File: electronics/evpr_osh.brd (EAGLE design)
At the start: 88.4 x 47.3 mm, 137 parts

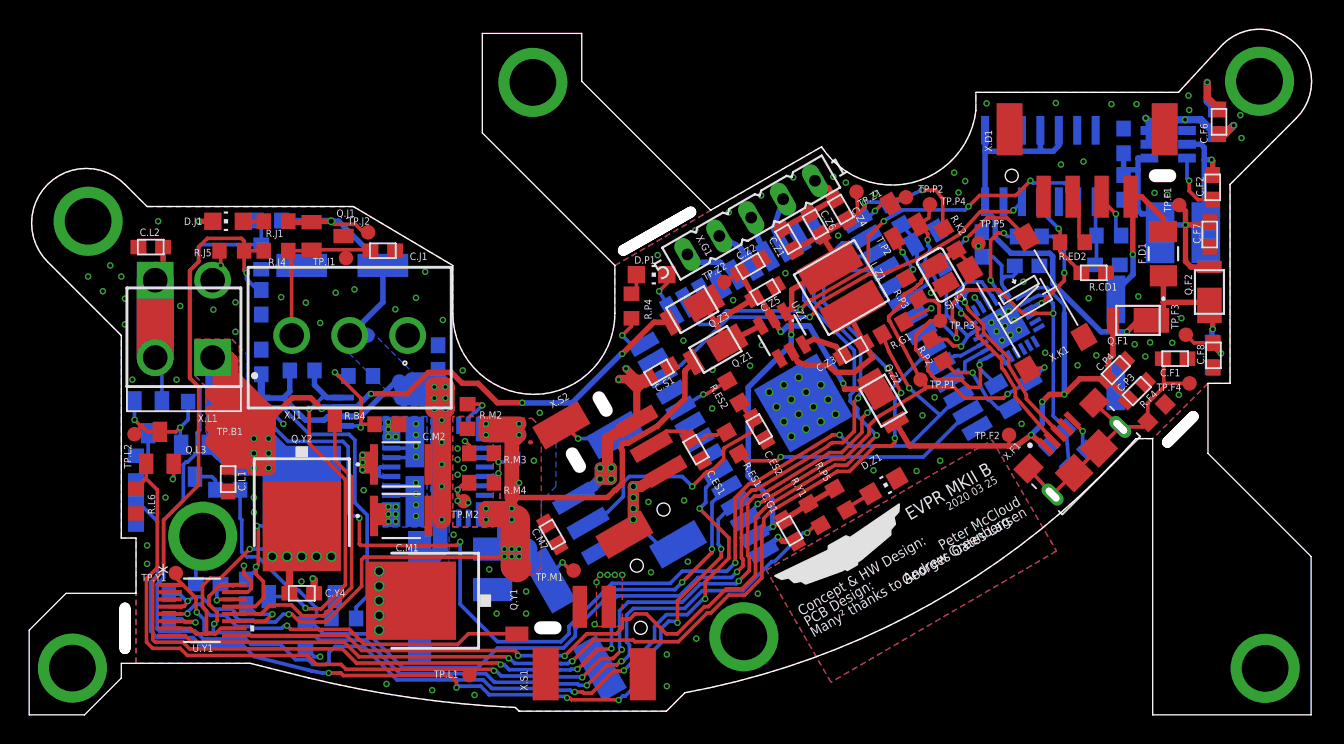
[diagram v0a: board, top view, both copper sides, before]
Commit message: Slightly squeezed board profile down
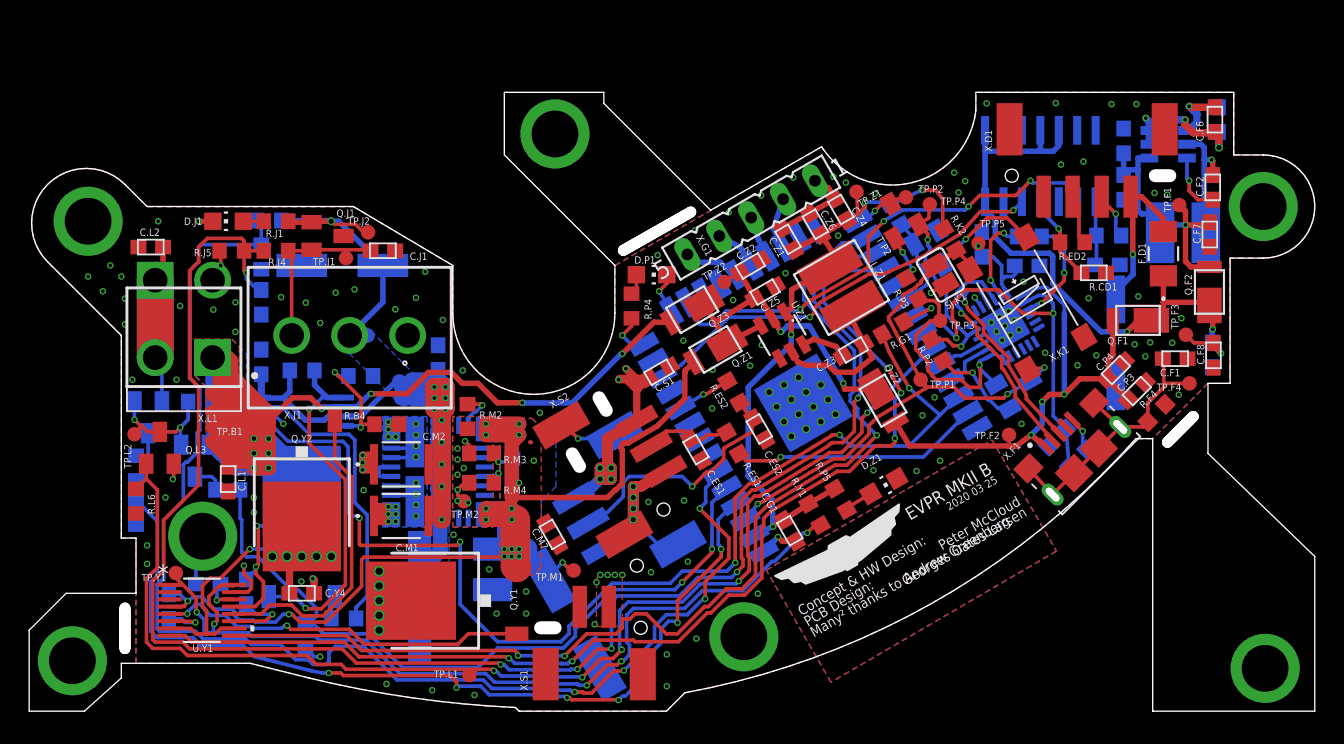
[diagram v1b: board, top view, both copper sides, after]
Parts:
- moved C.F6 0.32 mm to (47.0, -15.3)
- moved C.F4 0.27 mm to (47.2, -15.3)
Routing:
- net GND: track 71.5 -> 73.3 mm, vias 163 -> 159
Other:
- board size 88.4 x 47.3 mm -> 88.6 x 42.7 mm
